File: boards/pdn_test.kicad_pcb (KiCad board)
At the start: 4 copper layers, 30 x 20 mm, 4 parts, among them U1 LOAD

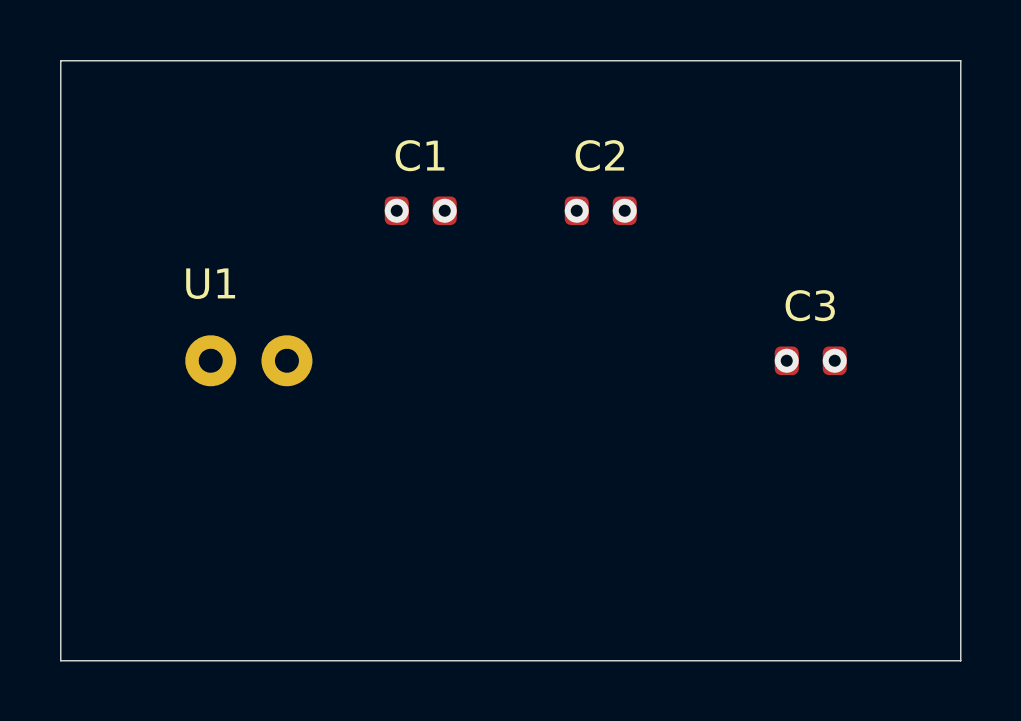
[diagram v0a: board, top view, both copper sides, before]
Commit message: Score the search at 100 kHz–30 MHz on a thin P/G coupon and restyle the plots.
The 1 GHz peak was VRM ESL, so the README looked like a miss. Hold 50 mΩ where MLCCs can actually fight it, and draw the VRM floor on the full-band overlay.

Co-authored-by: markomij12 <markomij12@users.noreply.github.com>
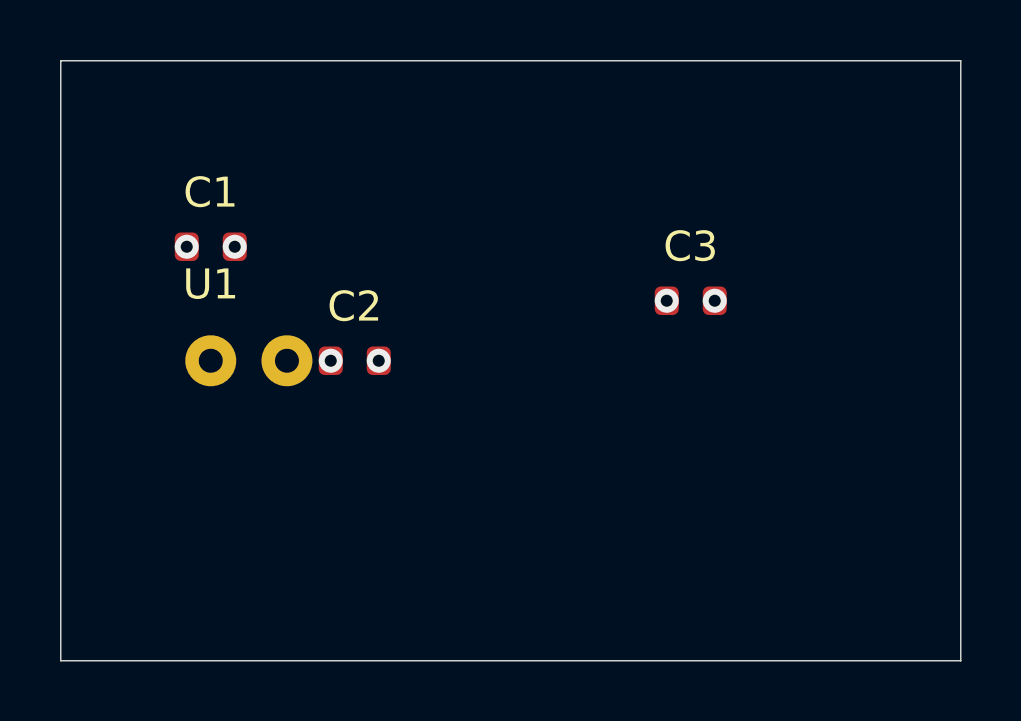
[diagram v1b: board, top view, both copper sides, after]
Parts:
- moved C2 9.60 mm to (9.80, 10.0)
- moved C1 7.10 mm to (5.00, 6.20)
- moved C3 4.47 mm to (21.0, 8.00)
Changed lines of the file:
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@@
 			)
 			(layer "dielectric 1"
-				(type "prepreg")
-				(thickness 0.2)
+				(type "core")
+				(thickness 1.04)
 				(material "FR4")
 				(epsilon_r 4.5)
@@
 			)
 			(layer "dielectric 2"
-				(type "core")
-				(thickness 1.04)
+				(type "prepreg")
+				(thickness 0.2)
 				(material "FR4")
 				(epsilon_r 4.5)
@@
 	(footprint "Capacitor_SMD:C_0603_1608Metric"
 		(layer "F.Cu")
-		(at 12 5)
+		(at 5 6.2)
 		(descr "Candidate decap C1")
 		(tags "pdn decap")
@@
 	(footprint "Capacitor_SMD:C_0603_1608Metric"
 		(layer "F.Cu")
-		(at 18 5)
+		(at 9.8 10)
 		(descr "Candidate decap C2")
 		(tags "pdn decap")
@@
 	(footprint "Capacitor_SMD:C_0603_1608Metric"
 		(layer "F.Cu")
-		(at 25 10)
+		(at 21 8)
 		(descr "Candidate decap C3")
 		(tags "pdn decap")
@@
 	)
 	(via
-		(at 11.2 5)
+		(at 4.2 6.2)
 		(size 0.8)
 		(drill 0.4)
@@
 	)
 	(via
-		(at 12.8 5)
+		(at 5.8 6.2)
 		(size 0.8)
 		(drill 0.4)
@@
 	)
 	(via
-		(at 17.2 5)
+		(at 9.0 10)
 		(size 0.8)
 		(drill 0.4)
@@
 	)
 	(via
-		(at 18.8 5)
+		(at 10.6 10)
 		(size 0.8)
 		(drill 0.4)
@@
 	)
 	(via
-		(at 24.2 10)
+		(at 20.2 8)
 		(size 0.8)
 		(drill 0.4)
@@
 	)
 	(via
-		(at 25.8 10)
-		(size 0.8)
-		(drill 0.4)
+		(at 21.8 8)
+		(size 0.8)
+		(drill 0.4)
